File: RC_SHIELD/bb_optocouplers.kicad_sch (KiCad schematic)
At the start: 17 parts, among them J15 Conn_01x04, J16 Conn_01x04, J17 Conn_01x04, U10 SFH6345, U4 SFH6345, U5 SFH6345, U6 SFH6345, U7 SFH6345, U8 SFH6345, U9 SFH6345

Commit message: added secondary MCU to schematic and made it more consistent
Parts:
- removed J15, J16, J17: Conn_01x04, Connector_RJ:RJ9_Evercom_5301-440xxx_Horizontal, symbol Connector_Generic:Conn_01x04
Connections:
- net Z_G_TOP_24: now reaches U4.2
- net Z_G_BOT_24: now reaches U5.2
- net SRV1_PWM_24: now reaches U8.6
- net SRV2_PWM_24: now reaches U9.6
- net SRV3_PWM_24: now reaches U10.6
- net R_G_IN_24: now reaches U6.2
- net R_G_OUT_24: now reaches U7.2
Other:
- note removed: "R Gates"
- note removed: "Servos"
- note removed: "Z gates"
- company: (none) -> LEGO Kör (legokor.hu)
- title: SERVOS, POSITION GATES -> Karcsi (INDACT Robot Arm) - Servo & position-gate optocouplers
- moved on the sheet: R17, R18, R19, U10, U8, U9

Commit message: footprints assigned
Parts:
- R13, R14, R15, R16, R17, R18, R19: footprint (none) -> Resistor_SMD:R_0805_2012Metric_Pad1.20x1.40mm_HandSolder
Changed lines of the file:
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@@
       (effects (font (size 1.27 1.27)) (justify left))
     )
-    (property "Footprint" "" (at 50.292 46.99 90)
+    (property "Footprint" "Resistor_SMD:R_0805_2012Metric_Pad1.20x1.40mm_HandSolder" (at 50.292 46.99 90)
       (effects (font (size 1.27 1.27)) hide)
     )
@@
       (effects (font (size 1.27 1.27)) (justify left))
     )
-    (property "Footprint" "" (at 50.292 181.61 90)
+    (property "Footprint" "Resistor_SMD:R_0805_2012Metric_Pad1.20x1.40mm_HandSolder" (at 50.292 181.61 90)
       (effects (font (size 1.27 1.27)) hide)
     )
@@
       (effects (font (size 1.27 1.27)) (justify left))
     )
-    (property "Footprint" "" (at 197.612 137.795 90)
+    (property "Footprint" "Resistor_SMD:R_0805_2012Metric_Pad1.20x1.40mm_HandSolder" (at 197.612 137.795 90)
       (effects (font (size 1.27 1.27)) hide)
     )
@@
       (effects (font (size 1.27 1.27)) (justify left))
     )
-    (property "Footprint" "" (at 198.882 90.805 90)
+    (property "Footprint" "Resistor_SMD:R_0805_2012Metric_Pad1.20x1.40mm_HandSolder" (at 198.882 90.805 90)
       (effects (font (size 1.27 1.27)) hide)
     )
@@
       (effects (font (size 1.27 1.27)) (justify left))
     )
-    (property "Footprint" "" (at 50.292 88.9 90)
+    (property "Footprint" "Resistor_SMD:R_0805_2012Metric_Pad1.20x1.40mm_HandSolder" (at 50.292 88.9 90)
       (effects (font (size 1.27 1.27)) hide)
     )
@@
       (effects (font (size 1.27 1.27)) (justify left))
     )
-    (property "Footprint" "" (at 50.292 134.62 90)
+    (property "Footprint" "Resistor_SMD:R_0805_2012Metric_Pad1.20x1.40mm_HandSolder" (at 50.292 134.62 90)
       (effects (font (size 1.27 1.27)) hide)
     )
@@
       (effects (font (size 1.27 1.27)) (justify left))
     )
-    (property "Footprint" "" (at 198.882 46.355 90)
-      (effects (font (size 1.27 1.27)) hide)
-    )
+    (property "Footprint" "Resistor_SMD:R_0805_2012Metric_Pad1.20x1.40mm_HandSolder" (at 198.882 46.355 90)
+      (effects (font (size 1.27 1.27)) hide)
+    )

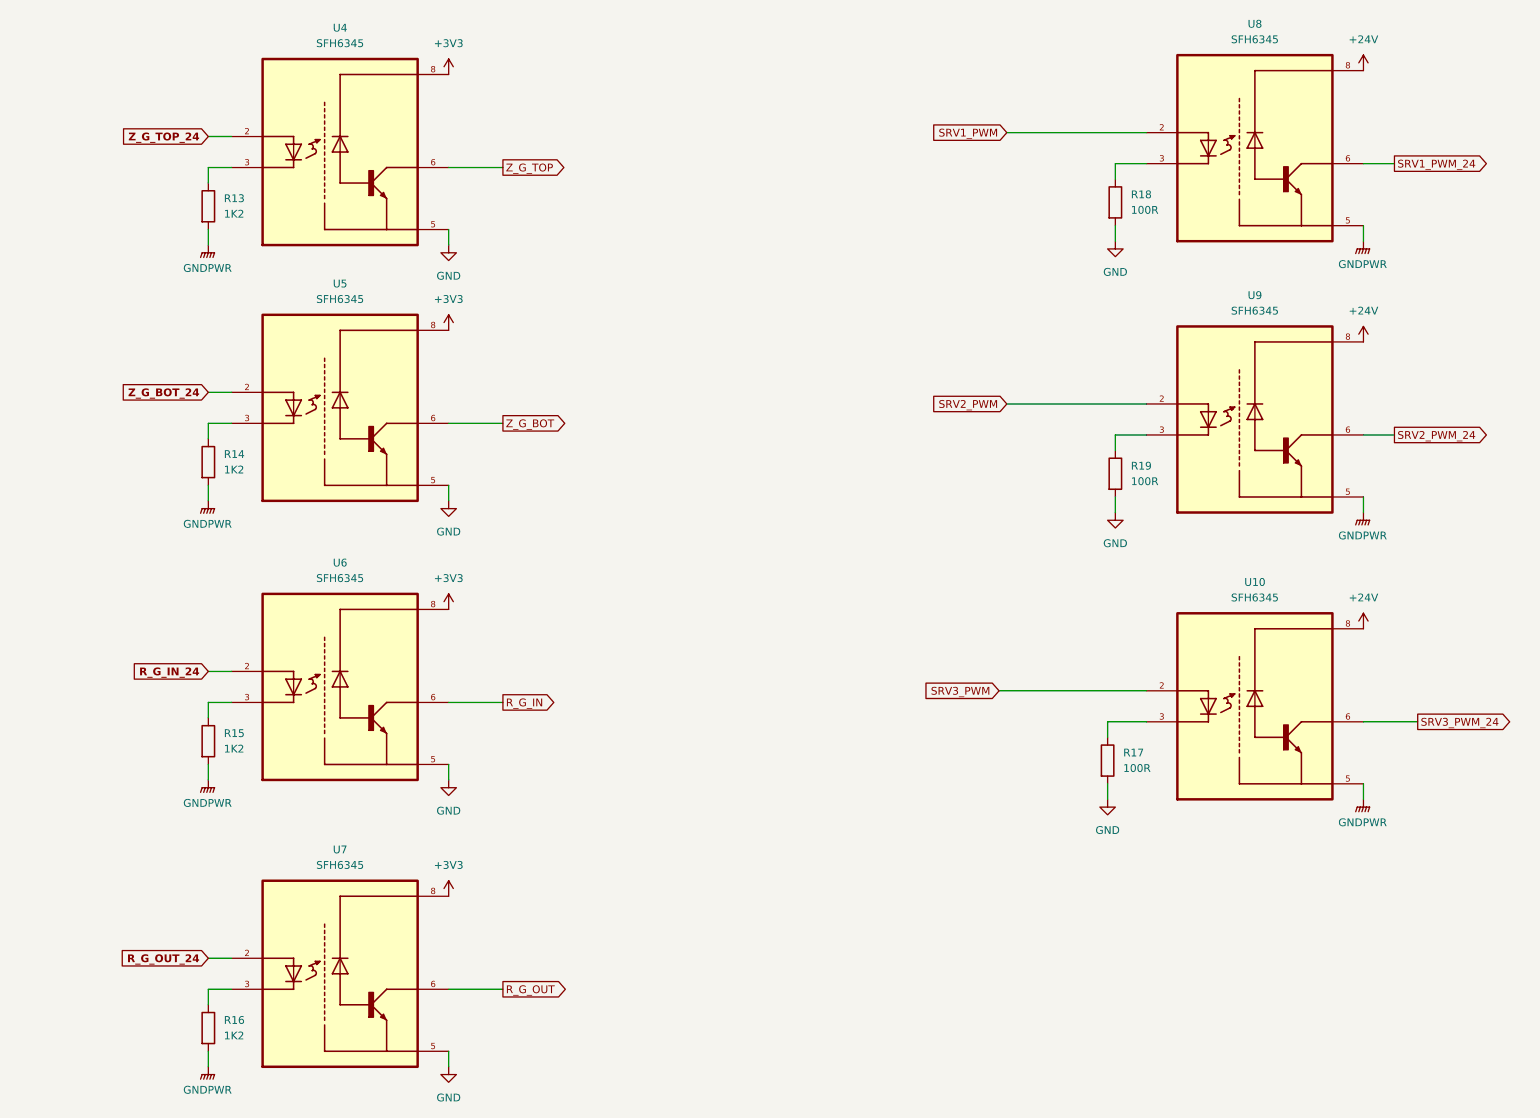
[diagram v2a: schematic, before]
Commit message: Fixed typos and names in schematic, changed optocoupler resistors; added .gitgnore file
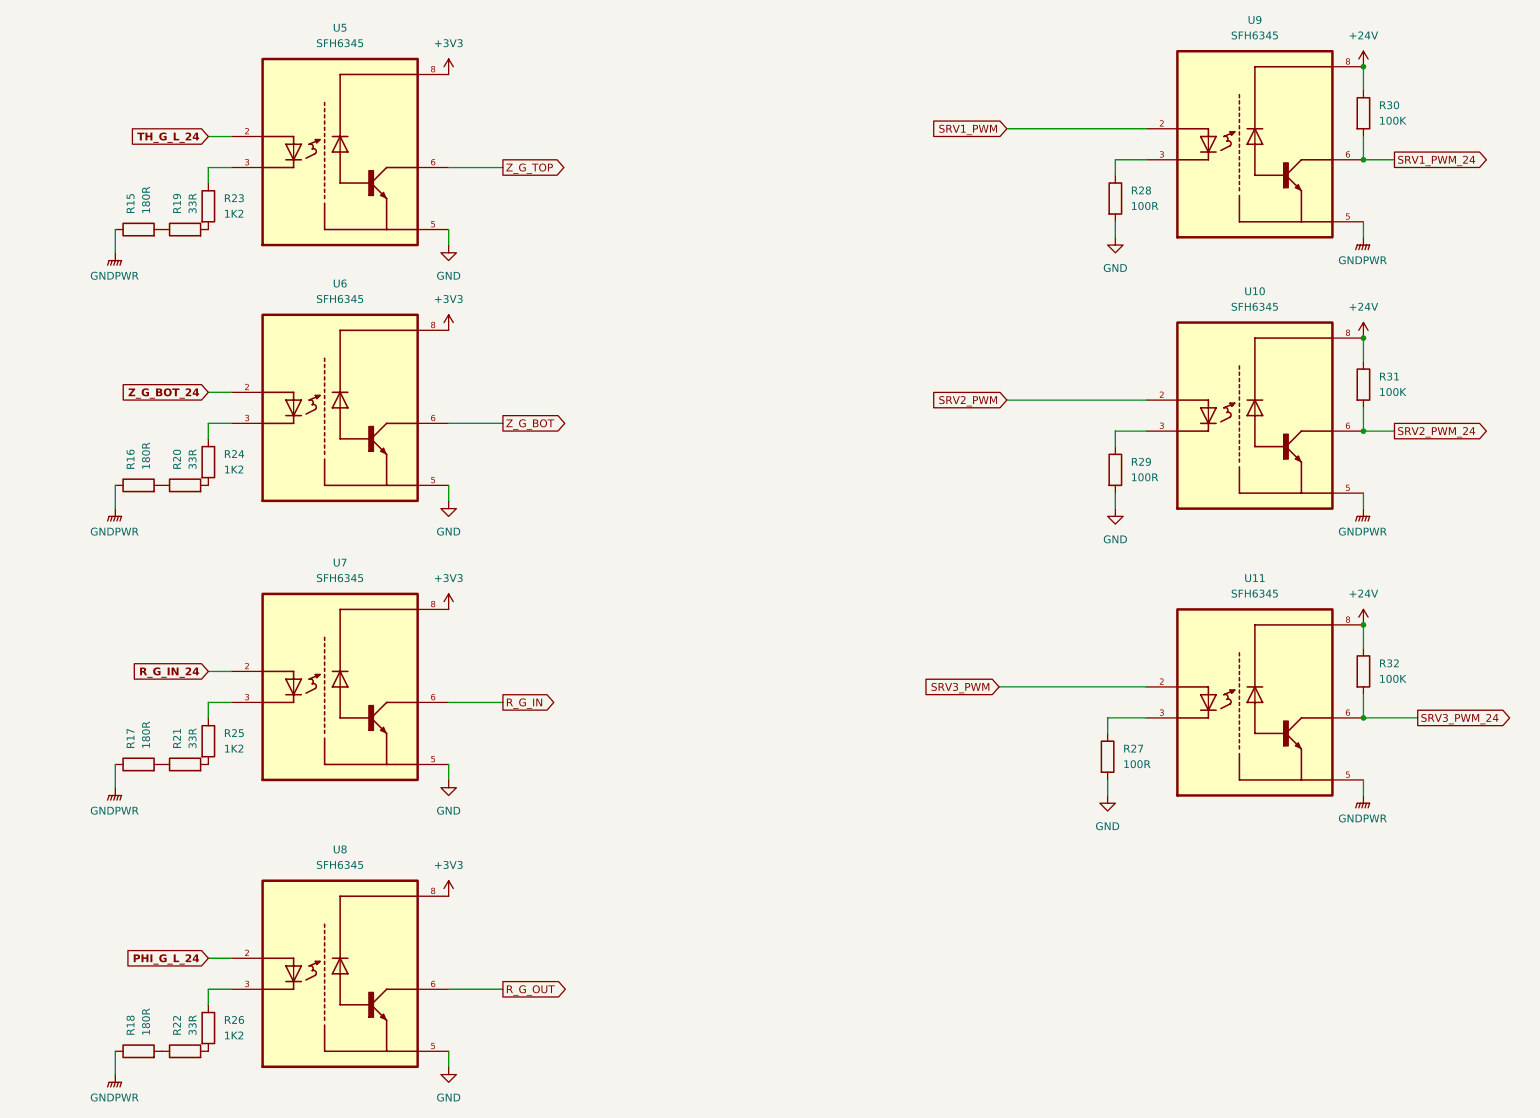
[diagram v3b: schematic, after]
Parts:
- removed R14: 1K2, Resistor_SMD:R_0805_2012Metric_Pad1.20x1.40mm_HandSolder, symbol Device:R
- added R17, R18: 180R, Resistor_SMD:R_0805_2012Metric_Pad1.20x1.40mm_HandSolder, symbol Device:R
- added R19, R20, R21, R22: 33R, Resistor_SMD:R_0805_2012Metric_Pad1.20x1.40mm_HandSolder, symbol Device:R
- added R24, R25, R26: 1K2, Resistor_SMD:R_0805_2012Metric_Pad1.20x1.40mm_HandSolder, symbol Device:R
- added R30, R31, R32: 100K, Resistor_SMD:R_0805_2012Metric_Pad1.20x1.40mm_HandSolder, symbol Device:R
- R15, R16: value 1K2 -> 180R
- renumbered R13 to R23, R17 to R27, R18 to R28, R19 to R29, U9 to U10, U10 to U11, U4 to U5, U5 to U6, U6 to U7, U7 to U8, U8 to U9
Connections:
- net +24V: now also R30.1, R31.1, R32.1
- net GNDPWR: now also R15.1, R16.1, R17.1, R18.1; no longer R15.2, R16.2, R23.2
- net SRV1_PWM_24: now also R30.2
- net SRV2_PWM_24: now also R31.2
- net SRV3_PWM_24: now also R32.2
- net at U8.3: now also R26.1; no longer R16.1
- net at U7.3: now also R25.1; no longer R15.1
- net at U6.3: now also R24.1
- net R_G_OUT_24 renamed PHI_G_L_24
- net Z_G_TOP_24 renamed TH_G_L_24
- new net: R17.2, R21.1
- new net: R19.2, R23.2
- new net: R16.2, R20.1
- new net: R15.2, R19.1
- new net: R21.2, R25.2
- new net: R20.2, R24.2
- new net: R18.2, R22.1
- new net: R22.2, R26.2
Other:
- moved on the sheet: R27, R28, R29, U10, U11, U9
